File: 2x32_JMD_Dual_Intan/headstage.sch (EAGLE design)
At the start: 22 parts

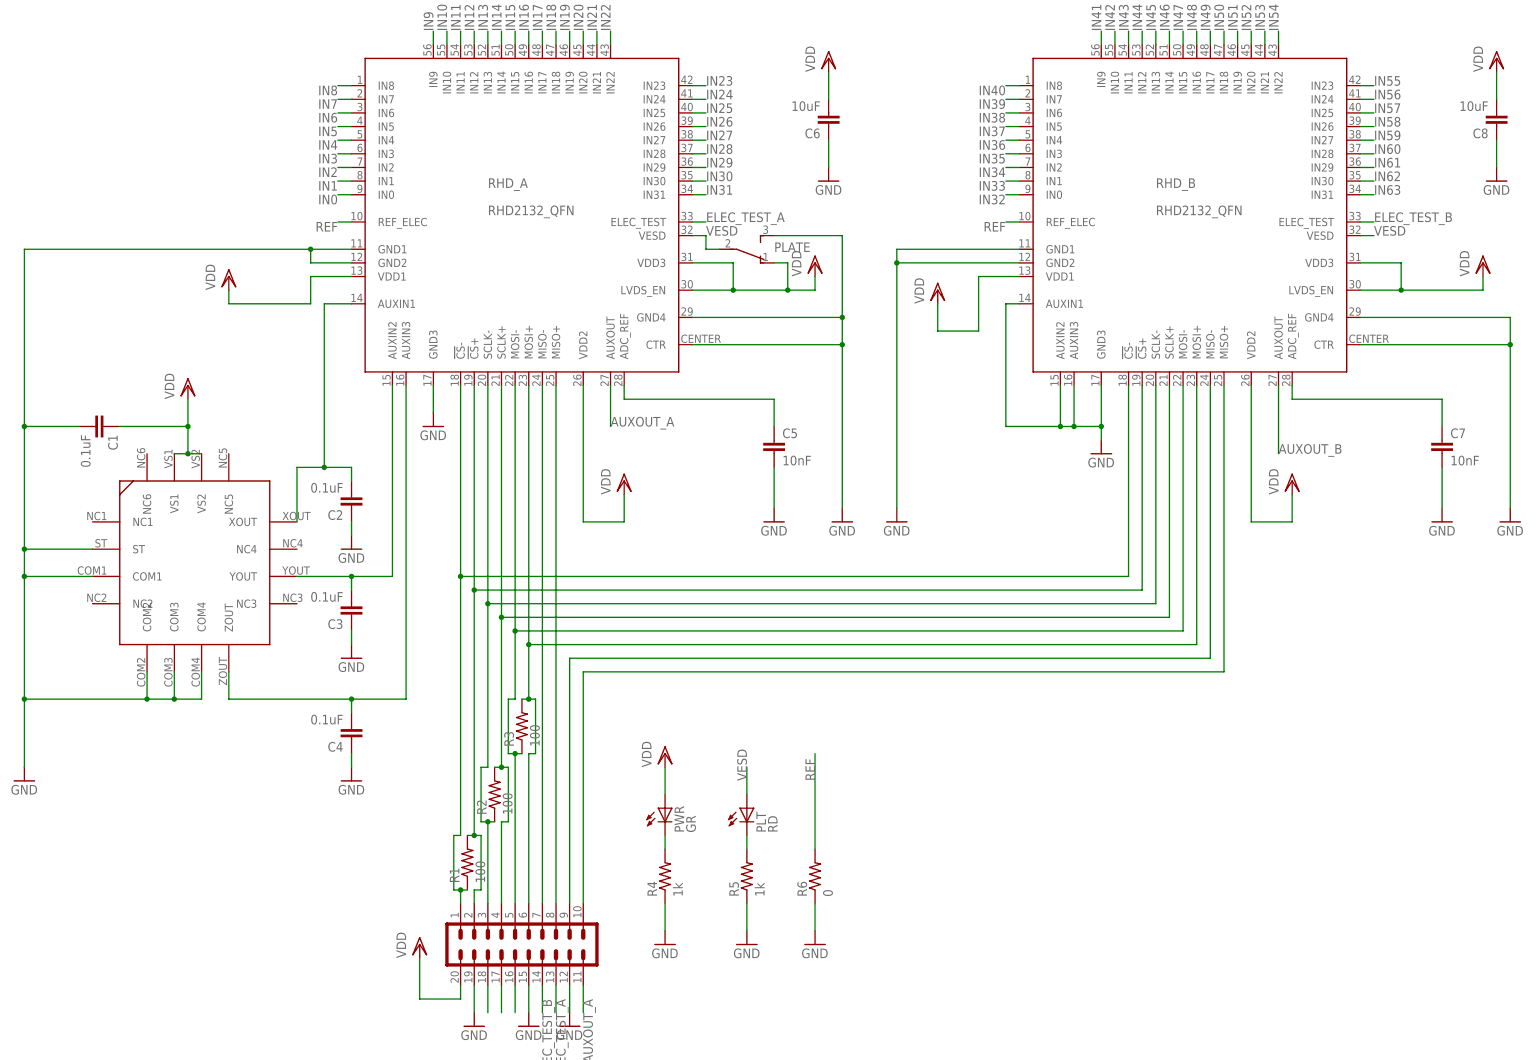
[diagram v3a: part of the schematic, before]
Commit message: Fixed the design rules for the JMD headstage to fit OSH park's new tolerances. Added a BOM.
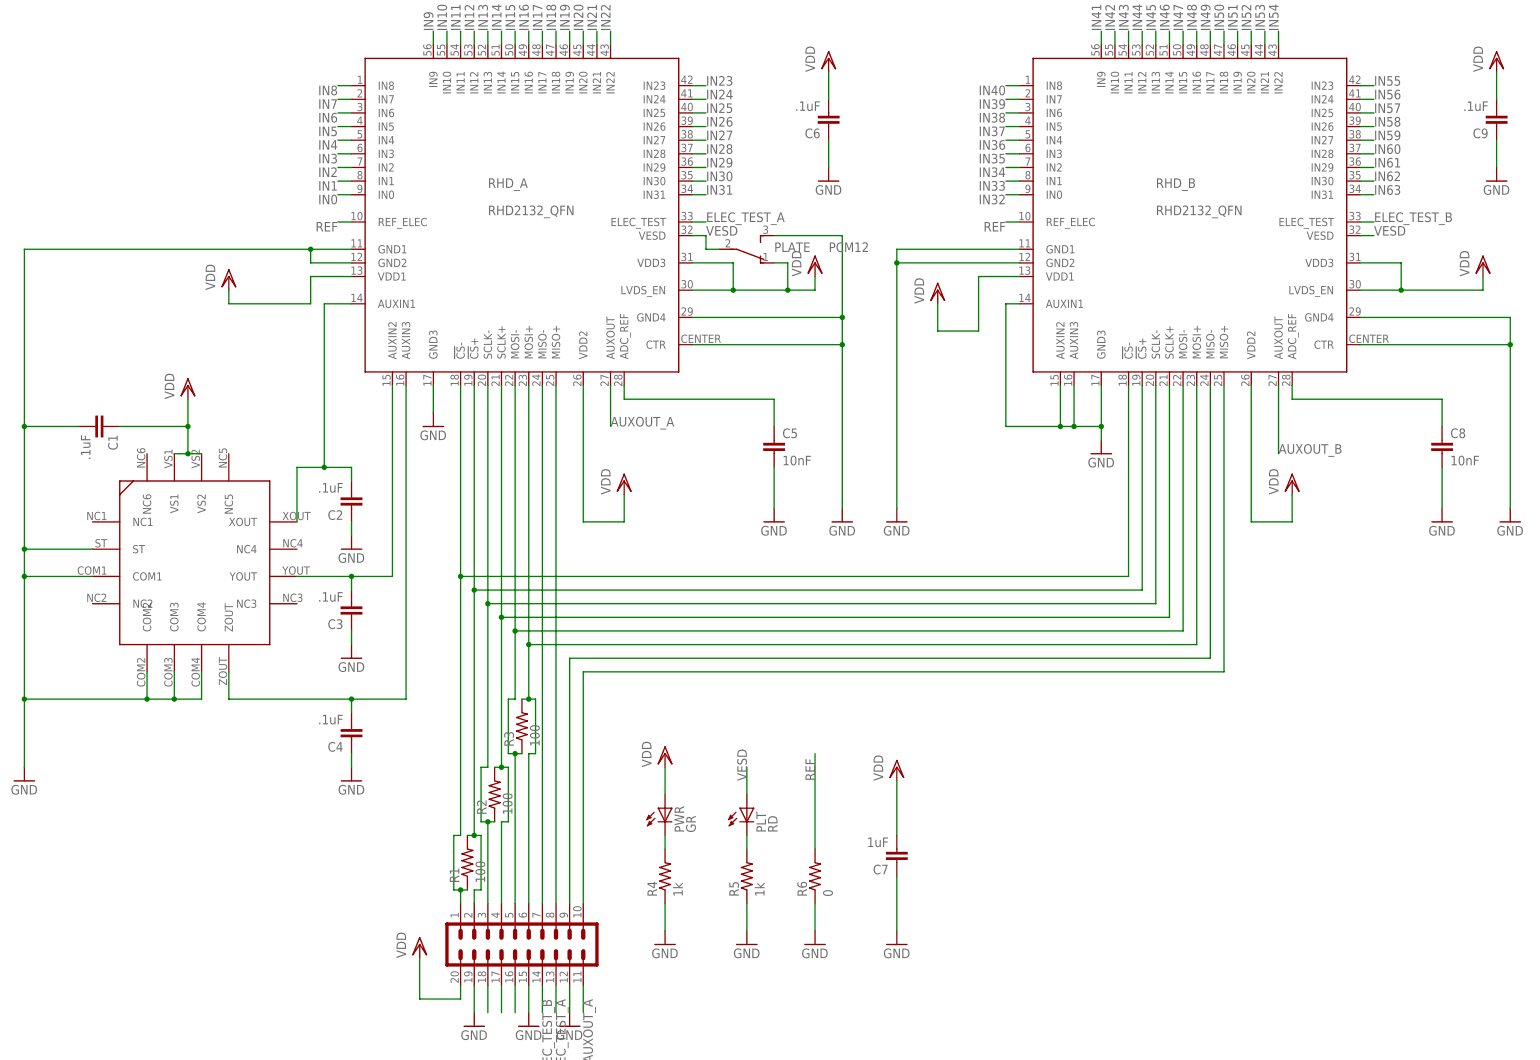
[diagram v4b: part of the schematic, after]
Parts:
- added C9: .1uF, headstage:C_0603
- C1, C2, C3, C4: value 0.1uF -> .1uF
- C6: value 10uF -> .1uF
- C7: value 10nF -> 1uF; device headstage:C_0402 -> headstage:C_0603
- C8: value 10uF -> 10nF; device headstage:C_0603 -> headstage:C_0402
- PLATE: value (none) -> PCM12
- renumbered U$1 to U1
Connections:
- net GND: now also C7.1, C8.2, C9.1; no longer C7.2, C8.1
- net N$3: now also C8.1; no longer C7.1
- net VDD: now also C7.2, C9.2; no longer C8.2
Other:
- moved on the sheet: C7, C8
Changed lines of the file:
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@@
 </classes>
 <parts>
-<part name="U$1" library="headstage" deviceset="ADXL335" device=""/>
+<part name="U1" library="headstage" deviceset="ADXL335" device=""/>
 <part name="RHD_A" library="headstage" deviceset="RHD2132" device="_QFN"/>
 <part name="R3" library="headstage" deviceset="R" device="_0402" value="100"/>
 <part name="R1" library="headstage" deviceset="R" device="_0402" value="100"/>
 <part name="R2" library="headstage" deviceset="R" device="_0402" value="100"/>
-<part name="C1" library="headstage" deviceset="C" device="_0402" value="0.1uF"/>
-<part name="C2" library="headstage" deviceset="C" device="_0402" value="0.1uF"/>
-<part name="C3" library="headstage" deviceset="C" device="_0402" value="0.1uF"/>
-<part name="C4" library="headstage" deviceset="C" device="_0402" value="0.1uF"/>
-<part name="C6" library="headstage" deviceset="C" device="_0603" value="10uF"/>
+<part name="C1" library="headstage" deviceset="C" device="_0402" value=".1uF"/>
+<part name="C2" library="headstage" deviceset="C" device="_0402" value=".1uF"/>
+<part name="C3" library="headstage" deviceset="C" device="_0402" value=".1uF"/>
+<part name="C4" library="headstage" deviceset="C" device="_0402" value=".1uF"/>
+<part name="C6" library="headstage" deviceset="C" device="_0603" value=".1uF"/>
 <part name="C5" library="headstage" deviceset="C" device="_0402" value="10nF"/>
 <part name="R4" library="headstage" deviceset="R" device="_0402" value="1k"/>
@@
 <part name="RHD_B" library="headstage" deviceset="RHD2132" device="_QFN"/>
 <part name="GND18" library="headstage" deviceset="GND" device=""/>
-<part name="C8" library="headstage" deviceset="C" device="_0603" value="10uF"/>
+<part name="C9" library="headstage" deviceset="C" device="_0603" value=".1uF"/>
 <part name="VDD13" library="headstage" deviceset="VDD" device=""/>
 <part name="GND19" library="headstage" deviceset="GND" device=""/>
-<part name="C7" library="headstage" deviceset="C" device="_0402" value="10nF"/>
+<part name="C8" library="headstage" deviceset="C" device="_0402" value="10nF"/>
 <part name="VDD15" library="headstage" deviceset="VDD" device=""/>
 <part name="GND24" library="headstage" deviceset="GND" device=""/>
@@
 <part name="PWR" library="puggleboard" deviceset="LED" device="_0603" value="GR"/>
 <part name="AIN" library="headstage" deviceset="PINHD-2X35" device="_JMD70" value="JMD70"/>
-<part name="PLATE" library="headstage" deviceset="SPDT" device="_PCM12"/>
+<part name="PLATE" library="headstage" deviceset="SPDT" device="_PCM12" value="PCM12"/>
 <part name="GND1" library="headstage" deviceset="GND" device=""/>
 <part name="R6" library="headstage" deviceset="R" device="_0402" value="0"/>
@@
 <part name="PLT" library="puggleboard" deviceset="LED" device="_0603" value="RD"/>
 <part name="FRAME1" library="headstage" deviceset="FRAME" device=""/>
+<part name="C7" library="headstage" deviceset="C" device="_0603" value="1uF"/>
+<part name="VDD2" library="headstage" deviceset="VDD" device=""/>
+<part name="GND7" library="headstage" deviceset="GND" device=""/>
 </parts>
 <sheets>
@@
 </plain>
 <instances>
-<instance part="U$1" gate="G$1" x="68.58" y="127"/>
+<instance part="U1" gate="G$1" x="68.58" y="127"/>
 <instance part="RHD_A" gate="A" x="132.08" y="190.5"/>
 <instance part="R3" gate="R" x="133.35" y="96.52" rot="R90"/>
@@
 <instance part="RHD_B" gate="A" x="256.54" y="190.5"/>
 <instance part="GND18" gate="1" x="180.34" y="134.62"/>
-<instance part="C8" gate="C" x="314.96" y="208.28" rot="R180"/>
+<instance part="C9" gate="C" x="314.96" y="208.28" rot="R180"/>
 <instance part="VDD13" gate="G$1" x="314.96" y="220.98"/>
 <instance part="GND19" gate="1" x="314.96" y="198.12"/>
-<instance part="C7" gate="C" x="304.8" y="149.86"/>
+<instance part="C8" gate="C" x="304.8" y="149.86"/>
 <instance part="VDD15" gate="G$1" x="312.42" y="182.88"/>
 <instance part="GND24" gate="1" x="317.5" y="134.62"/>
@@
 <instance part="PLATE" gate="G$1" x="172.72" y="185.42" smashed="yes" rot="MR180">
 <attribute name="NAME" x="180.34" y="186.69" size="1.778" layer="95" rot="MR180"/>
-<attribute name="VALUE" x="172.72" y="194.31" size="1.778" layer="96" rot="MR180"/>
+<attribute name="VALUE" x="190.5" y="186.69" size="1.778" layer="96" rot="MR180"/>
 </instance>
 <instance part="GND1" gate="1" x="152.4" y="248.92"/>
@@
 <instance part="FRAME1" gate="G$1" x="0" y="0"/>
 <instance part="FRAME1" gate="G$2" x="271.78" y="0"/>
+<instance part="C7" gate="C" x="203.2" y="71.12" rot="R180"/>
+<instance part="VDD2" gate="G$1" x="203.2" y="88.9"/>
+<instance part="GND7" gate="1" x="203.2" y="55.88"/>
 </instances>
 <busses>
@@
 </segment>
 <segment>
-<pinref part="U$1" gate="G$1" pin="COM3"/>
+<pinref part="U1" gate="G$1" pin="COM3"/>
 <wire x1="68.58" y1="106.68" x2="68.58" y2="101.6" width="0.1524" layer="91"/>
-<pinref part="U$1" gate="G$1" pin="COM2"/>
+<pinref part="U1" gate="G$1" pin="COM2"/>
 <wire x1="63.5" y1="106.68" x2="63.5" y2="101.6" width="0.1524" layer="91"/>
 <wire x1="63.5" y1="101.6" x2="40.64" y2="101.6" width="0.1524" layer="91"/>
@@
 <junction x="68.58" y="101.6"/>
 <wire x1="73.66" y1="101.6" x2="68.58" y2="101.6" width="0.1524" layer="91"/>
-<pinref part="U$1" gate="G$1" pin="COM4"/>
+<pinref part="U1" gate="G$1" pin="COM4"/>
 <wire x1="73.66" y1="106.68" x2="73.66" y2="101.6" width="0.1524" layer="91"/>
 <pinref part="GND30" gate="1" pin="GND"/>
@@
 <wire x1="40.64" y1="129.54" x2="40.64" y2="152.4" width="0.1524" layer="91"/>
 <wire x1="40.64" y1="152.4" x2="50.8" y2="152.4" width="0.1524" layer="91"/>
-<pinref part="U$1" gate="G$1" pin="ST"/>
+<pinref part="U1" gate="G$1" pin="ST"/>
 <wire x1="53.34" y1="129.54" x2="40.64" y2="129.54" width="0.1524" layer="91"/>
 <junction x="40.64" y="129.54"/>
-<pinref part="U$1" gate="G$1" pin="COM1"/>
+<pinref part="U1" gate="G$1" pin="COM1"/>
 <wire x1="53.34" y1="124.46" x2="40.64" y2="124.46" width="0.1524" layer="91"/>
 <junction x="40.64" y="124.46"/>
@@
 <segment>
 <pinref part="GND19" gate="1" pin="GND"/>
-<pinref part="C8" gate="C" pin="1"/>
+<pinref part="C9" gate="C" pin="1"/>
 <wire x1="314.96" y1="205.74" x2="314.96" y2="200.66" width="0.1524" layer="91"/>
 </segment>
@@
 </segment>
 <segment>
-<pinref part="C7" gate="C" pin="2"/>
+<pinref part="C8" gate="C" pin="2"/>
 <wire x1="304.8" y1="144.78" x2="304.8" y2="137.16" width="0.1524" layer="91"/>
 <pinref part="GND25" gate="1" pin="GND"/>
@@
 <pinref part="GND6" gate="1" pin="GND"/>
 </segment>
+<segment>
+<pinref part="GND7" gate="1" pin="GND"/>
+<pinref part="C7" gate="C" pin="1"/>
+<wire x1="203.2" y1="68.58" x2="203.2" y2="58.42" width="0.1524" layer="91"/>
+</segment>
 </net>
 <net name="REF" class="0">
@@
 </segment>
 <segment>
-<pinref part="U$1" gate="G$1" pin="VS1"/>
-<pinref part="U$1" gate="G$1" pin="VS2"/>
+<pinref part="U1" gate="G$1" pin="VS1"/>
+<pinref part="U1" gate="G$1" pin="VS2"/>
 <wire x1="68.58" y1="147.32" x2="71.12" y2="147.32" width="0.1524" layer="91"/>
 <wire x1="71.12" y1="147.32" x2="73.66" y2="147.32" width="0.1524" layer="91"/>
@@
 </segment>
 <segment>
-<pinref part="C8" gate="C" pin="2"/>
+<pinref part="C9" gate="C" pin="2"/>
 <pinref part="VDD13" gate="G$1" pin="VDD"/>
 <wire x1="314.96" y1="213.36" x2="314.96" y2="218.44" width="0.1524" layer="91"/>
@@
 <wire x1="121.92" y1="45.72" x2="121.92" y2="48.26" width="0.1524" layer="91"/>
 </segment>
+<segment>
+<pinref part="VDD2" gate="G$1" pin="VDD"/>
+<pinref part="C7" gate="C" pin="2"/>
+<wire x1="203.2" y1="76.2" x2="203.2" y2="86.36" width="0.1524" layer="91"/>
+</segment>
 </net>
 <net name="XOUT1" class="0">
@@
 <wire x1="96.52" y1="175.26" x2="96.52" y2="144.78" width="0.1524" layer="91"/>
 <wire x1="96.52" y1="144.78" x2="91.44" y2="144.78" width="0.1524" layer="91"/>
-<pinref part="U$1" gate="G$1" pin="XOUT"/>
+<pinref part="U1" gate="G$1" pin="XOUT"/>
 <wire x1="91.44" y1="144.78" x2="91.44" y2="134.62" width="0.1524" layer="91"/>
 <pinref part="C2" gate="C" pin="2"/>
@@
 <wire x1="109.22" y1="160.02" x2="109.22" y2="124.46" width="0.1524" layer="91"/>
 <wire x1="109.22" y1="124.46" x2="101.6" y2="124.46" width="0.1524" layer="91"/>
-<pinref part="U$1" gate="G$1" pin="YOUT"/>
+<pinref part="U1" gate="G$1" pin="YOUT"/>
 <wire x1="101.6" y1="124.46" x2="91.44" y2="124.46" width="0.1524" layer="91"/>
 <pinref part="C3" gate="C" pin="2"/>
@@
 <wire x1="111.76" y1="160.02" x2="111.76" y2="101.6" width="0.1524" layer="91"/>
 <wire x1="111.76" y1="101.6" x2="101.6" y2="101.6" width="0.1524" layer="91"/>
-<pinref part="U$1" gate="G$1" pin="ZOUT"/>
+<pinref part="U1" gate="G$1" pin="ZOUT"/>
 <wire x1="101.6" y1="101.6" x2="78.74" y2="101.6" width="0.1524" layer="91"/>
 <wire x1="78.74" y1="101.6" x2="78.74" y2="106.68" width="0.1524" layer="91"/>
@@
 <net name="N$3" class="0">
 <segment>
-<pinref part="C7" gate="C" pin="1"/>
+<pinref part="C8" gate="C" pin="1"/>
 <wire x1="304.8" y1="152.4" x2="304.8" y2="157.48" width="0.1524" layer="91"/>
 <pinref part="RHD_B" gate="A" pin="ADC_REF"/>
